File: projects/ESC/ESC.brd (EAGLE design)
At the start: 139.7 x 38.1 mm, 92 parts, among them J1 1755529, J2 1755529, J3 1755529, J4 1755529, U1 STM32F405RGT6, U10 CSD88584Q5DCT, U11 CSD88584Q5DCT, U12 CSD88584Q5DCT, U13 CSD88584Q5DCT, U2 CSD88584Q5DCT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

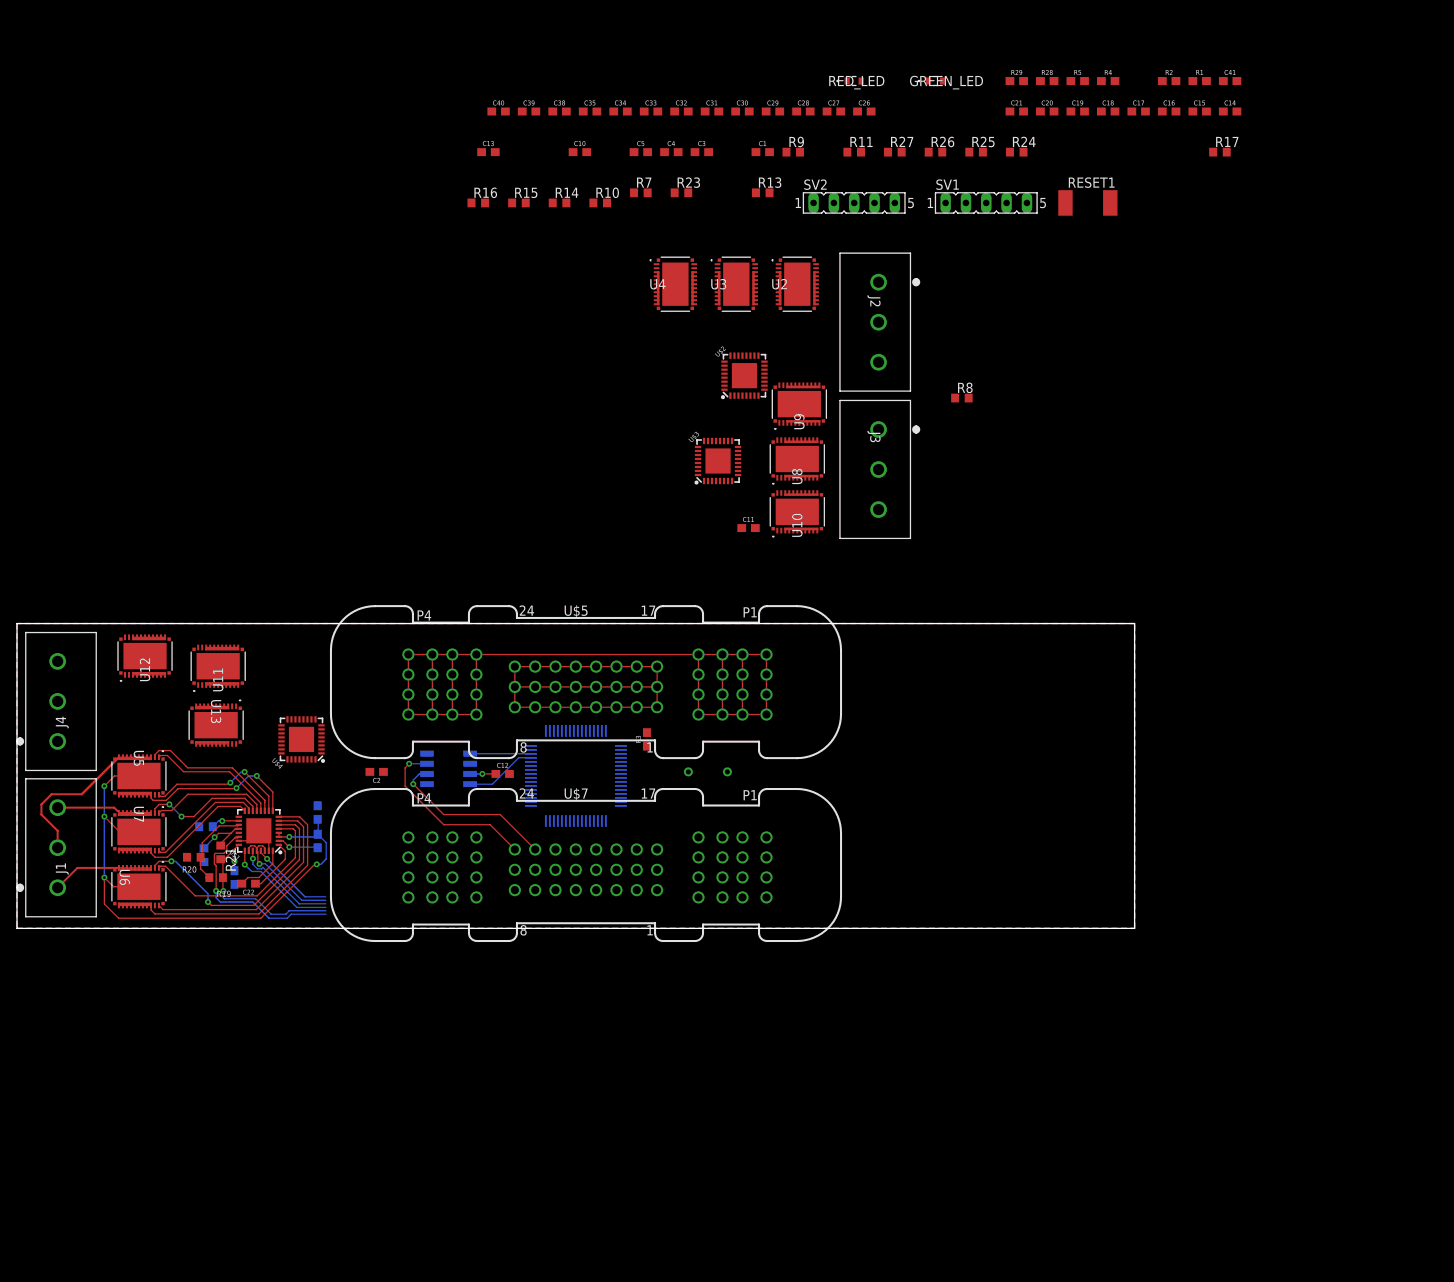
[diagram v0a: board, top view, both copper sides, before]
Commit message: layout of one esc
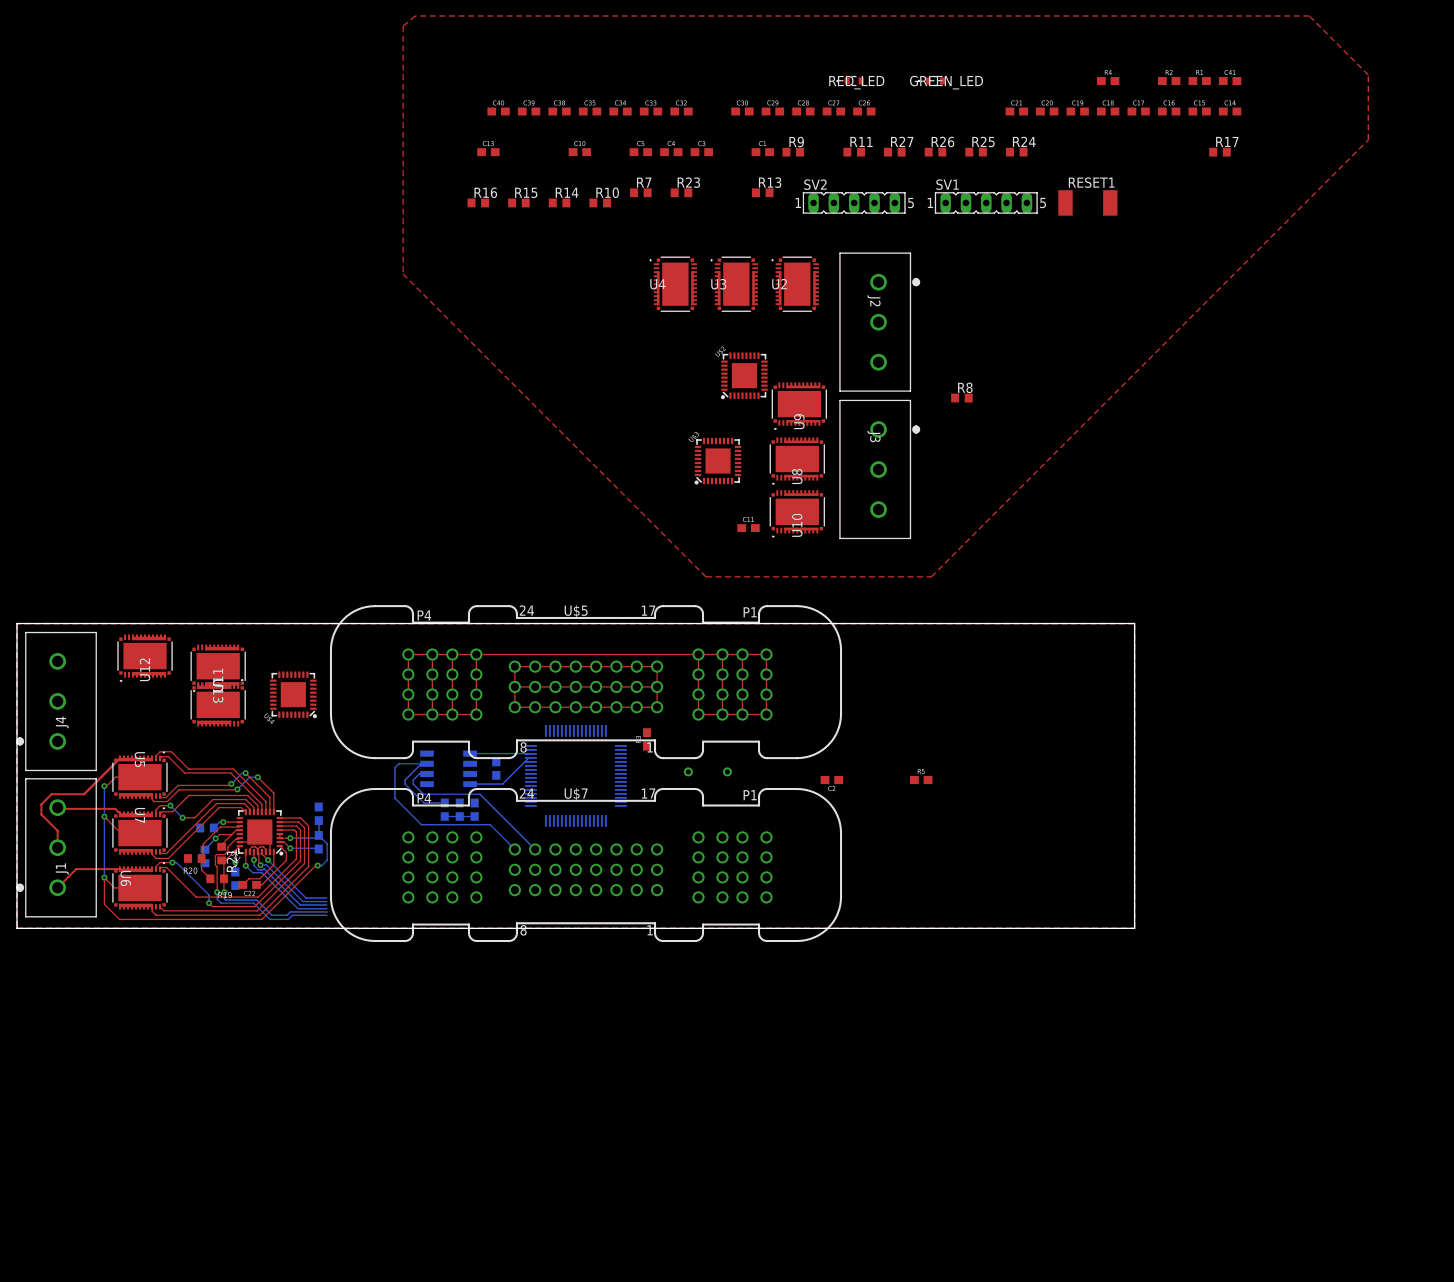
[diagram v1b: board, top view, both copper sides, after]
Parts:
- moved R28 118.2 mm to (53.5, 14.8), flipped to the bottom, turned to 90 degrees
- moved R29 113.5 mm to (57.2, 14.8), flipped to the bottom, turned to 270 degrees
- moved C31 92.8 mm to (55.3, 14.8), flipped to the bottom, turned to 270 degrees
- moved R5 89.5 mm to (113.0, 18.5)
- moved C2 56.9 mm to (101.9, 18.5)
- moved U$4 5.68 mm to (34.5, 29.2)
- moved U13 2.55 mm to (25.1, 27.9)
- moved C12 1.03 mm to (59.9, 20.0), flipped to the bottom, turned to 90 degrees
- moved C24 0.20 mm to (37.7, 14.3)
- moved C25 0.20 mm to (37.7, 10.8)
- moved R20 0.20 mm to (22.2, 8.74)
- moved R22 0.20 mm to (23.5, 8.99)
- moved U$1 0.20 mm to (30.4, 12.0)
- moved U5 0.20 mm to (15.4, 18.9)
- moved U6 0.20 mm to (15.4, 5.05)
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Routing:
- net CAN_H: track 22.2 -> 35.0 mm, vias 1 -> 0
- net N$46: track 0.00 -> 3.73 mm
- net +3V3: track 3.21 -> 0.00 mm, vias 1 -> 0
- net VM_2: track 72.0 -> 72.7 mm
- net CAN_L: vias 1 -> 0

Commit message: made wires thicker
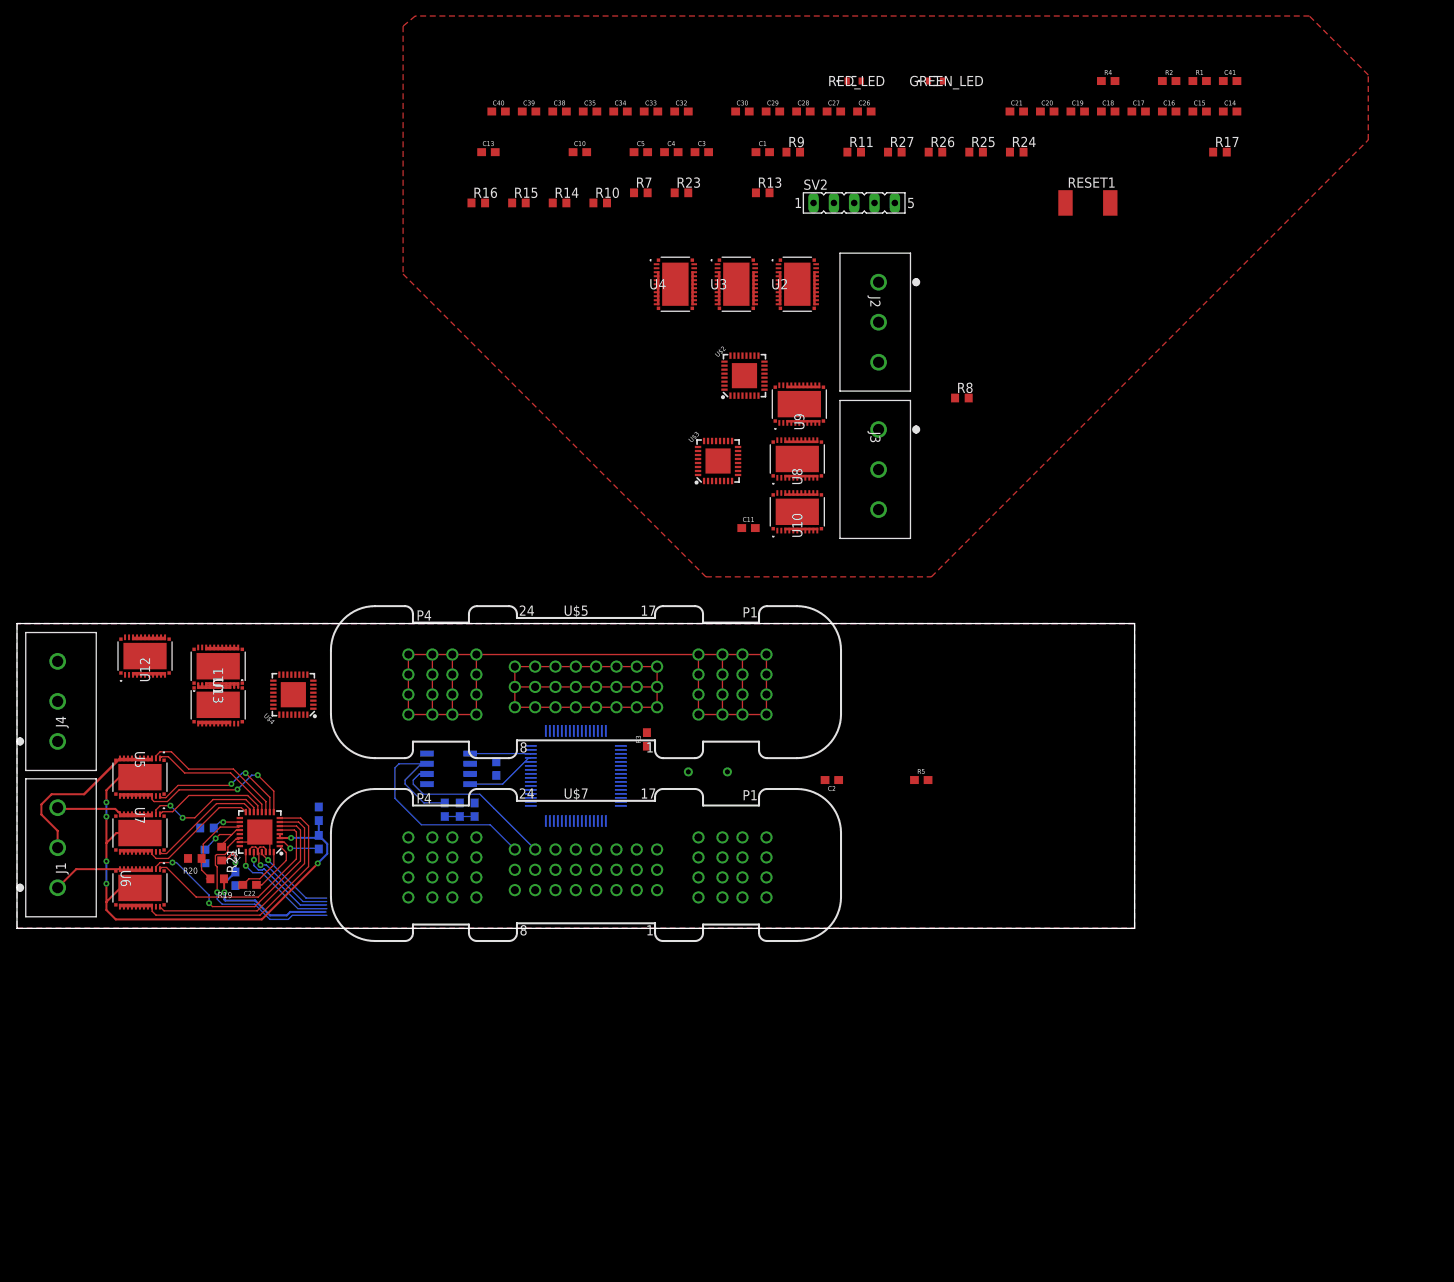
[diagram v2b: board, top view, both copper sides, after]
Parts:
- removed SV1: (no value), con-lsta:FE05-1
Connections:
- new net DVDD_2: C23.1, R19.2, R21.2, U$1.24
- net +3V3: no longer SV1.5
- net 12V: no longer C23.1, R10.2, R19.2, R21.2, R8.2, U$1.24
- net DVDD_1: now also R10.2, R8.2
- net GND: no longer SV1.3
- net NRST: no longer SV1.1
- net SWCLK: no longer SV1.4
- net SWDIO: no longer SV1.2
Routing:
- net 12V: track 146.9 -> 121.9 mm, vias 2 -> 0
- net DVDD_2: track 0.00 -> 23.6 mm, vias 0 -> 2
- net VM_2: track 72.7 -> 71.2 mm, vias 5 -> 6

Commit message: starting motor 1 (finished motor 2)
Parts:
- moved C14 42.6 mm to (123.2, 70.4)
- moved C15 38.8 mm to (125.5, 70.4)
- moved C17 37.3 mm to (123.4, 68.8)
- moved R10 16.6 mm to (57.9, 83.6)
- moved U13 10.8 mm to (15.4, 32.5)
- moved C24 8.59 mm to (37.6, 5.74), turned to 270 degrees
- moved U12 8.41 mm to (15.4, 25.7), turned to 270 degrees
- moved U$4 4.38 mm to (33.8, 24.9)
- moved U11 3.76 mm to (24.4, 29.1)
- moved J1 0.80 mm to (5.84, 5.33), flipped to the bottom
- moved J4 0.76 mm to (5.84, 23.4), flipped to the bottom
- moved U5 0.10 mm to (15.4, 18.8)
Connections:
- net N$15 renamed PHASE_A2
- new net SLC_1B: U4.12, U4.13, U4.14, U4.15, U4.16, U4.17, U4.18, U4.19, U4.20
- net GHB_1: now also U4.1; no longer U2.1
- net GHC_1: now also U2.1; no longer U4.1
- net GLB_1: now also U4.22; no longer U2.22
- net GLC_1: now also U2.22; no longer U4.22
- net PHASE_B1: now also U4.10, U4.11, U4.3, U4.4, U4.5, U4.6, U4.7, U4.8, U4.9; no longer U2.10, U2.11, U2.3, U2.4, U2.5, U2.6, U2.7, U2.8, U2.9
- net PHASE_C1: now also U2.10, U2.11, U2.3, U2.4, U2.5, U2.6, U2.7, U2.8, U2.9; no longer U4.10, U4.11, U4.3, U4.4, U4.5, U4.6, U4.7, U4.8, U4.9
- net SHB_1: now also U4.2; no longer U2.2
- net SHC_1: now also U2.2; no longer U4.2
- net SLB_1: no longer U2.12, U2.13, U2.14, U2.15, U2.16, U2.17, U2.18, U2.19, U2.20
- net SLC_1: now also U2.12, U2.13, U2.14, U2.15, U2.16, U2.17, U2.18, U2.19, U2.20; no longer U4.12, U4.13, U4.14, U4.15, U4.16, U4.17, U4.18, U4.19, U4.20
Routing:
- net 12V: track 121.9 -> 0.15 mm
- net 3V3: track 63.6 -> 0.00 mm
- net PHASE_B2: track 22.5 -> 17.7 mm
- net DVDD_2: track 23.6 -> 24.9 mm
- net GLB_2: track 18.2 -> 17.4 mm
- net PHASE_A2: track 12.7 -> 12.0 mm
- net PHASE_C2: track 15.0 -> 14.4 mm
- net SHC_2: track 15.6 -> 15.0 mm
- added copper zone on layer 1, net 12V
- added copper zone on layer 1, net 12V1
- added copper zone on layer 1, net 3V3
